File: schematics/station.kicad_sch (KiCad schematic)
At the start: 15 parts, among them J1 USB_C_Receptacle, J2 Conn_01x04_Pin, J3 Conn_02x05_Odd_Even, SW1 SW_Push, U1 ESP32-C3-MINI-1, U4 AP2112K-3.3

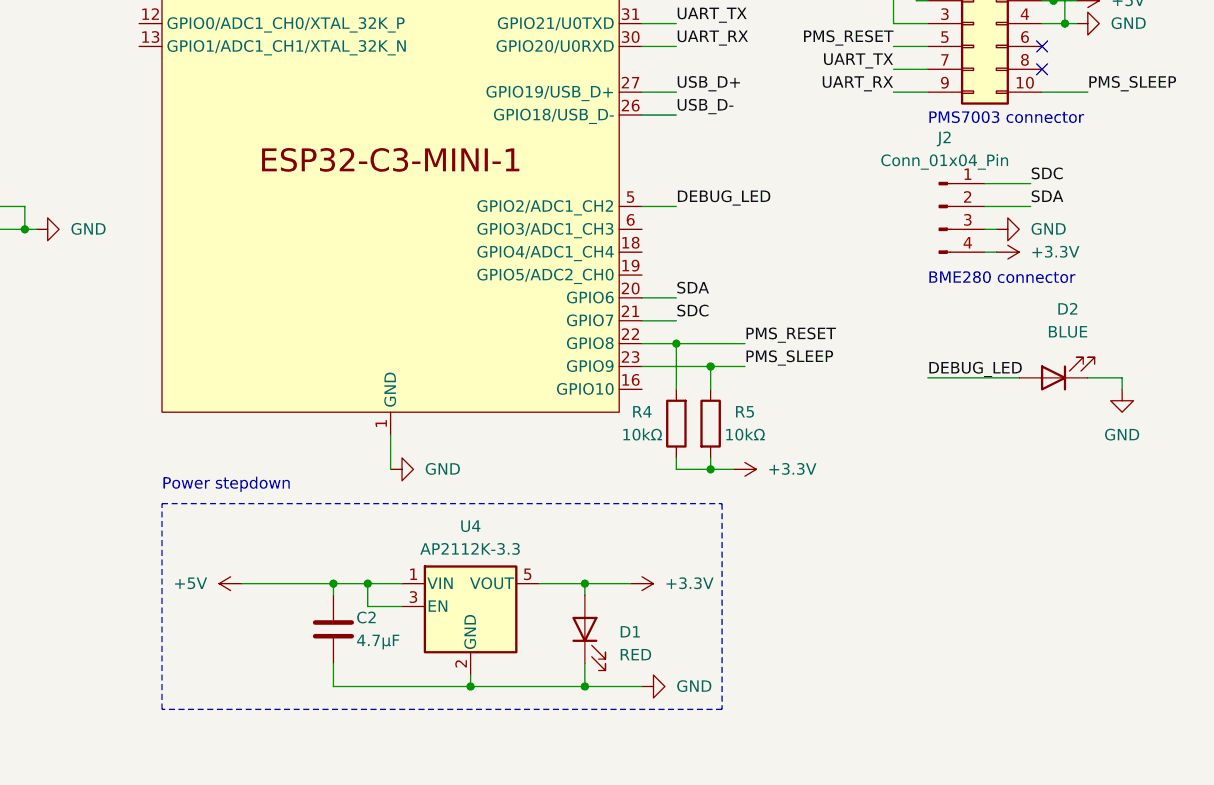
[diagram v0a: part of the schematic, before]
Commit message: Added another decoupling capacitor
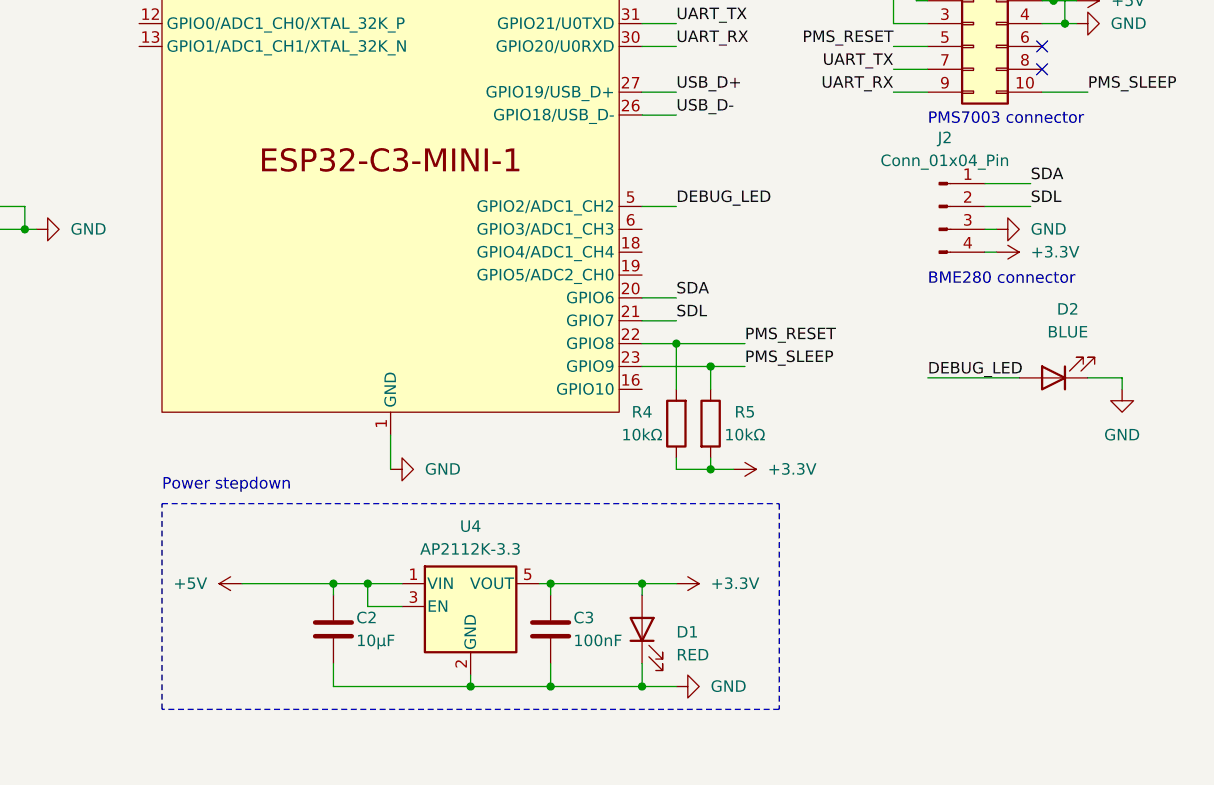
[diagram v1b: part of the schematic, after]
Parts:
- added C3: 100nF, Capacitor_SMD:C_0805_2012Metric_Pad1.18x1.45mm_HandSolder, symbol Device:C
- C2: value 4.7µF -> 10µF
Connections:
- net +3.3V: now also C3.1
- net GND: now also C3.2
- net SDA: now also J2.1 (Pin_1); no longer J2.2 (Pin_2)
- net SDC renamed SDL
- net SDL: now also J2.2 (Pin_2); no longer J2.1 (Pin_1)
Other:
- moved on the sheet: D1
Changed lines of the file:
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@@
     (comment 1 "pkozak.org")
   )
+  (junction (at 129.54 116.84) (diameter 0) (color 0 0 0 0)
+  )
   (junction (at 110.49 128.27) (diameter 0) (color 0 0 0 0)
   )
+  (junction (at 119.38 116.84) (diameter 0) (color 0 0 0 0)
+  )
   (junction (at 60.96 77.47) (diameter 0) (color 0 0 0 0)
   )
@@
   (junction (at 175.26 52.07) (diameter 0) (color 0 0 0 0)
   )
-  (junction (at 123.19 116.84) (diameter 0) (color 0 0 0 0)
+  (junction (at 119.38 128.27) (diameter 0) (color 0 0 0 0)
   )
   (junction (at 21.59 135.89) (diameter 0) (color 0 0 0 0)
@@
   (junction (at 95.25 116.84) (diameter 0) (color 0 0 0 0)
   )
-  (junction (at 123.19 128.27) (diameter 0) (color 0 0 0 0)
+  (junction (at 129.54 128.27) (diameter 0) (color 0 0 0 0)
   )
   (no_connect (at 44.45 110.49))
@@
     (stroke (width 0) (type default))
   )
-  (wire (pts (xy 123.19 125.73) (xy 123.19 128.27))
+  (wire (pts (xy 129.54 125.73) (xy 129.54 128.27))
     (stroke (width 0) (type default))
   )
@@
     (stroke (width 0) (type default))
   )
-  (wire (pts (xy 123.19 118.11) (xy 123.19 116.84))
+  (wire (pts (xy 129.54 118.11) (xy 129.54 116.84))
     (stroke (width 0) (type default))
   )
@@
     (stroke (width 0) (type default))
   )
+  (wire (pts (xy 133.35 116.84) (xy 129.54 116.84))
+    (stroke (width 0) (type default))
+  )
   (wire (pts (xy 129.54 92.71) (xy 137.16 92.71))
     (stroke (width 0) (type default))
   )
+  (wire (pts (xy 119.38 118.11) (xy 119.38 116.84))
+    (stroke (width 0) (type default))
+  )
   (wire (pts (xy 45.72 49.53) (xy 48.26 49.53))
     (stroke (width 0) (type default))
@@
     (stroke (width 0) (type default))
   )
-  (wire (pts (xy 110.49 128.27) (xy 123.19 128.27))
-    (stroke (width 0) (type default))
-  )
   (wire (pts (xy 71.12 40.64) (xy 73.66 40.64))
     (stroke (width 0) (type default))
@@
     (stroke (width 0) (type default))
   )
-  (wire (pts (xy 118.11 116.84) (xy 123.19 116.84))
+  (wire (pts (xy 118.11 116.84) (xy 119.38 116.84))
     (stroke (width 0) (type default))
   )
@@
     (stroke (width 0) (type default))
   )
-  (wire (pts (xy 123.19 128.27) (xy 129.54 128.27))
-    (stroke (width 0) (type default))
-  )
   (wire (pts (xy 176.53 54.61) (xy 177.8 54.61))
     (stroke (width 0) (type default))
@@
     (stroke (width 0) (type default))
   )
+  (wire (pts (xy 129.54 128.27) (xy 133.35 128.27))
+    (stroke (width 0) (type default))
+  )
   (wire (pts (xy 110.49 127) (xy 110.49 128.27))
     (stroke (width 0) (type default))
   )
+  (wire (pts (xy 119.38 116.84) (xy 129.54 116.84))
+    (stroke (width 0) (type default))
+  )
   (wire (pts (xy 179.07 93.98) (xy 182.88 93.98))
     (stroke (width 0) (type default))
@@
     (stroke (width 0) (type default))
   )
+  (wire (pts (xy 119.38 125.73) (xy 119.38 128.27))
+    (stroke (width 0) (type default))
+  )
   (wire (pts (xy 44.45 95.25) (xy 41.91 95.25))
     (stroke (width 0) (type default))
@@
     (stroke (width 0) (type default))
   )
+  (wire (pts (xy 110.49 128.27) (xy 119.38 128.27))
+    (stroke (width 0) (type default))
+  )
   (wire (pts (xy 55.88 77.47) (xy 60.96 77.47))
     (stroke (width 0) (type default))
@@
     (stroke (width 0) (type default))
   )
+  (wire (pts (xy 119.38 128.27) (xy 129.54 128.27))
+    (stroke (width 0) (type default))
+  )
   (wire (pts (xy 129.54 85.09) (xy 133.35 85.09))
     (stroke (width 0) (type default))
@@
     (stroke (width 0) (type default))
   )
-  (wire (pts (xy 123.19 116.84) (xy 128.27 116.84))
-    (stroke (width 0) (type default))
-  )
   (wire (pts (xy 175.26 49.53) (xy 160.02 49.53))
     (stroke (width 0) (type default))
@@
     (stroke (width 0) (type default))
   )
-  (rectangle (start 76.2 107.95) (end 138.43 130.81)
+  (rectangle (start 76.2 107.95) (end 144.78 130.81)
     (stroke (width 0) (type dash))
     (fill (type none))
@@
     (effects (font (size 1.27 1.27)) (justify left bottom))
   )
-  (label "SDC" (at 133.35 87.63 0) (fields_autoplaced)
-    (effects (font (size 1.27 1.27)) (justify left bottom))
-  )
-  (label "SDA" (at 172.72 74.93 0) (fields_autoplaced)
+  (label "SDL" (at 133.35 87.63 0) (fields_autoplaced)
+    (effects (font (size 1.27 1.27)) (justify left bottom))
+  )
+  (label "SDL" (at 172.72 74.93 0) (fields_autoplaced)
     (effects (font (size 1.27 1.27)) (justify left bottom))
   )
@@
     (effects (font (size 1.27 1.27)) (justify left bottom))
   )
-  (label "SDC" (at 172.72 72.39 0) (fields_autoplaced)
+  (label "SDA" (at 172.72 72.39 0) (fields_autoplaced)
     (effects (font (size 1.27 1.27)) (justify left bottom))
   )
@@
     (effects (font (size 1.27 1.27)) (justify left bottom))
   )
-  (symbol (lib_id "power:+3.3V") (at 128.27 116.84 270) (unit 1)
-    (in_bom yes) (on_board yes) (dnp no) (fields_autoplaced)
-    (property "Reference" "#PWR015" (at 124.46 116.84 0)
-      (effects (font (size 1.27 1.27)) hide)
-    )
-    (property "Value" "+3.3V" (at 132.08 116.84 90)
+  (symbol (lib_id "power:+3.3V") (at 133.35 116.84 270) (unit 1)
+    (in_bom yes) (on_board yes) (dnp no) (fields_autoplaced)
+    (property "Reference" "#PWR015" (at 129.54 116.84 0)
+      (effects (font (size 1.27 1.27)) hide)
+    )
+    (property "Value" "+3.3V" (at 137.16 116.84 90)
       (effects (font (size 1.27 1.27)) (justify left))
     )
-    (property "Footprint" "" (at 128.27 116.84 0)
-      (effects (font (size 1.27 1.27)) hide)
-    )
-    (property "Datasheet" "" (at 128.27 116.84 0)
+    (property "Footprint" "" (at 133.35 116.84 0)
+      (effects (font (size 1.27 1.27)) hide)
+    )
+    (property "Datasheet" "" (at 133.35 116.84 0)
       (effects (font (size 1.27 1.27)) hide)
     )
@@
     )
   )
+  (symbol (lib_id "Device:C") (at 119.38 121.92 0) (unit 1)
+    (in_bom yes) (on_board yes) (dnp no)
+    (property "Reference" "C3" (at 121.92 120.65 0)
+      (effects (font (size 1.27 1.27)) (justify left))
+    )
+    (property "Value" "100nF" (at 121.92 123.19 0)
+      (effects (font (size 1.27 1.27)) (justify left))
+    )
+    (property "Footprint" "Capacitor_SMD:C_0805_2012Metric_Pad1.18x1.45mm_HandSolder" (at 120.3452 125.73 0)
+      (effects (font (size 1.27 1.27)) hide)
+    )
+    (property "Datasheet" "~" (at 119.38 121.92 0)
+      (effects (font (size 1.27 1.27)) hide)
+    )
+    (pin "1")
+    (pin "2")
+    (instances
+      (project "station"
+        (path "/85aeb712-90fa-4269-bdea-e9fbee3a2d37"
+          (reference "C3") (unit 1)
+        )
+      )
+    )
+  )
   (symbol (lib_id "Device:R") (at 137.16 99.06 0) (unit 1)
     (in_bom yes) (on_board yes) (dnp no)
@@
     )
   )
-  (symbol (lib_id "Device:LED") (at 123.19 121.92 90) (unit 1)
-    (in_bom yes) (on_board yes) (dnp no) (fields_autoplaced)
-    (property "Reference" "D1" (at 127 122.2375 90)
+  (symbol (lib_id "Device:LED") (at 129.54 121.92 90) (unit 1)
+    (in_bom yes) (on_board yes) (dnp no) (fields_autoplaced)
+    (property "Reference" "D1" (at 133.35 122.2375 90)
       (effects (font (size 1.27 1.27)) (justify right))
     )
-    (property "Value" "RED" (at 127 124.7775 90)
+    (property "Value" "RED" (at 133.35 124.7775 90)
       (effects (font (size 1.27 1.27)) (justify right))
     )
-    (property "Footprint" "LED_SMD:LED_0805_2012Metric_Pad1.15x1.40mm_HandSolder" (at 123.19 121.92 0)
-      (effects (font (size 1.27 1.27)) hide)
-    )
-    (property "Datasheet" "~" (at 123.19 121.92 0)
+    (property "Footprint" "LED_SMD:LED_0805_2012Metric_Pad1.15x1.40mm_HandSolder" (at 129.54 121.92 0)
+      (effects (font (size 1.27 1.27)) hide)
+    )
+    (property "Datasheet" "~" (at 129.54 121.92 0)
       (effects (font (size 1.27 1.27)) hide)
     )
@@
       (effects (font (size 1.27 1.27)) (justify left))
     )
-    (property "Value" "4.7µF" (at 97.79 123.19 0)
+    (property "Value" "10µF" (at 97.79 123.19 0)
       (effects (font (size 1.27 1.27)) (justify left))
     )
@@
     )
   )
-  (symbol (lib_id "power:GND") (at 129.54 128.27 90) (unit 1)
-    (in_bom yes) (on_board yes) (dnp no) (fields_autoplaced)
-    (property "Reference" "#PWR014" (at 135.89 128.27 0)
-      (effects (font (size 1.27 1.27)) hide)
-    )
-    (property "Value" "GND" (at 133.35 128.27 90)
+  (symbol (lib_id "power:GND") (at 133.35 128.27 90) (unit 1)
+    (in_bom yes) (on_board yes) (dnp no) (fields_autoplaced)
+    (property "Reference" "#PWR014" (at 139.7 128.27 0)
+      (effects (font (size 1.27 1.27)) hide)
+    )
+    (property "Value" "GND" (at 137.16 128.27 90)
       (effects (font (size 1.27 1.27)) (justify right))
     )
-    (property "Footprint" "" (at 129.54 128.27 0)
-      (effects (font (size 1.27 1.27)) hide)
-    )
-    (property "Datasheet" "" (at 129.54 128.27 0)
-      (effects (font (size 1.27 1.27)) hide)
-    )
+    (property "Footprint" "" (at 133.35 128.27 0)
+      (effects (font (size 1.27 1.27)) hide)
+    )
+    (property "Datasheet" "" (at 133.35 128.27 0)
+      (effects (font (size 1.27 1.27)) hide)
+    )

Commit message: Some clarity changes and minor refactors
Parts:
- renumbered U4 to U2
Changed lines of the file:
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@@
   (symbol (lib_id "Regulator_Linear:AP2112K-3.3") (at 110.49 119.38 0) (unit 1)
     (in_bom yes) (on_board yes) (dnp no) (fields_autoplaced)
-    (property "Reference" "U4" (at 110.49 110.49 0)
+    (property "Reference" "U2" (at 110.49 110.49 0)
       (effects (font (size 1.27 1.27)))
     )
@@
       (project "station"
         (path "/85aeb712-90fa-4269-bdea-e9fbee3a2d37"
-          (reference "U4") (unit 1)
+          (reference "U2") (unit 1)
         )
       )
